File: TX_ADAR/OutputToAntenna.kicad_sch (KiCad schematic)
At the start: 8 parts, among them J10 Conn_Coaxial, J3 Conn_Coaxial, J4 Conn_Coaxial, J5 Conn_Coaxial, J6 Conn_Coaxial, J7 Conn_Coaxial, J8 Conn_Coaxial, J9 Conn_Coaxial

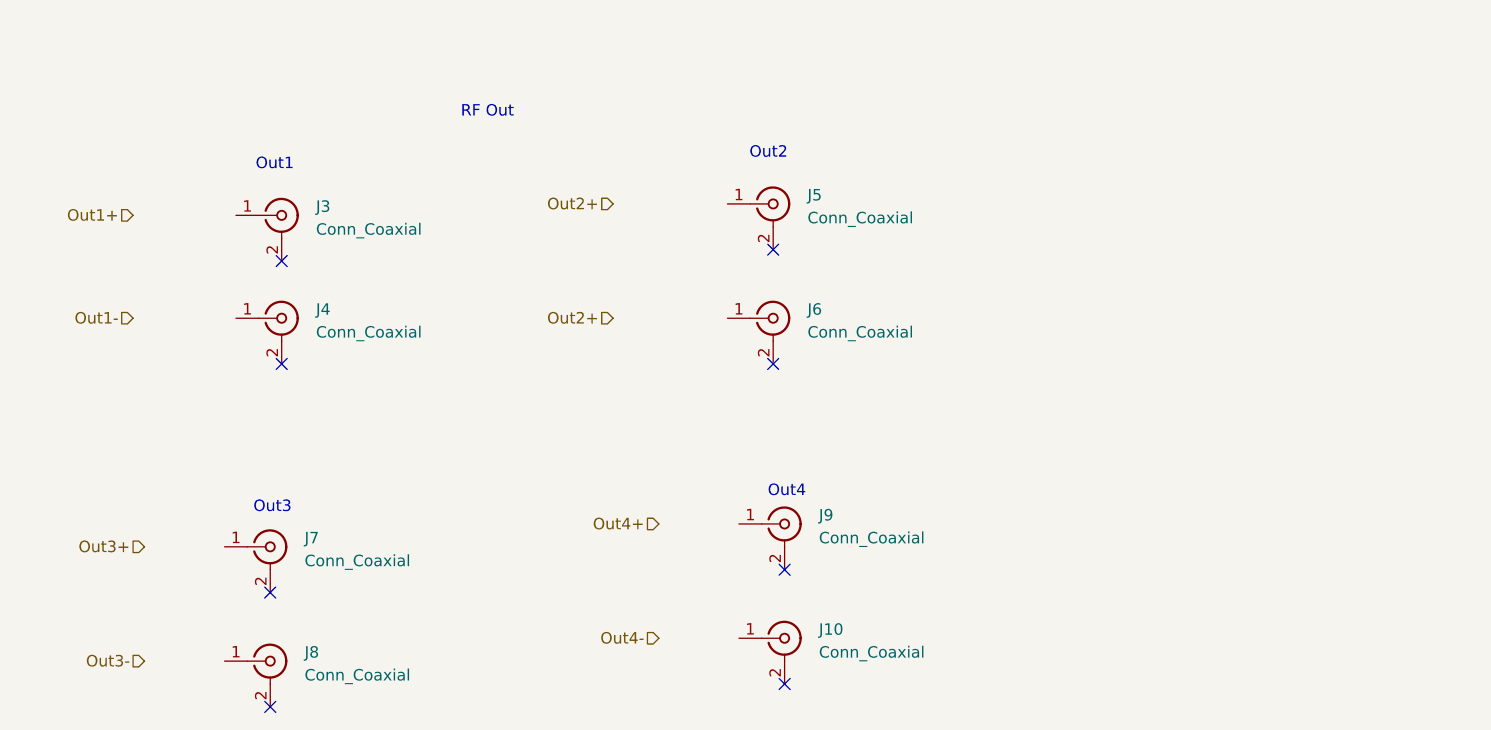
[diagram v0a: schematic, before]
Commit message: Cleaning up schematic
Added Cal Line
Connected RFOuts to connectors
Worked on State Machine connections
Finished connecting SDP Connector (need to double check)
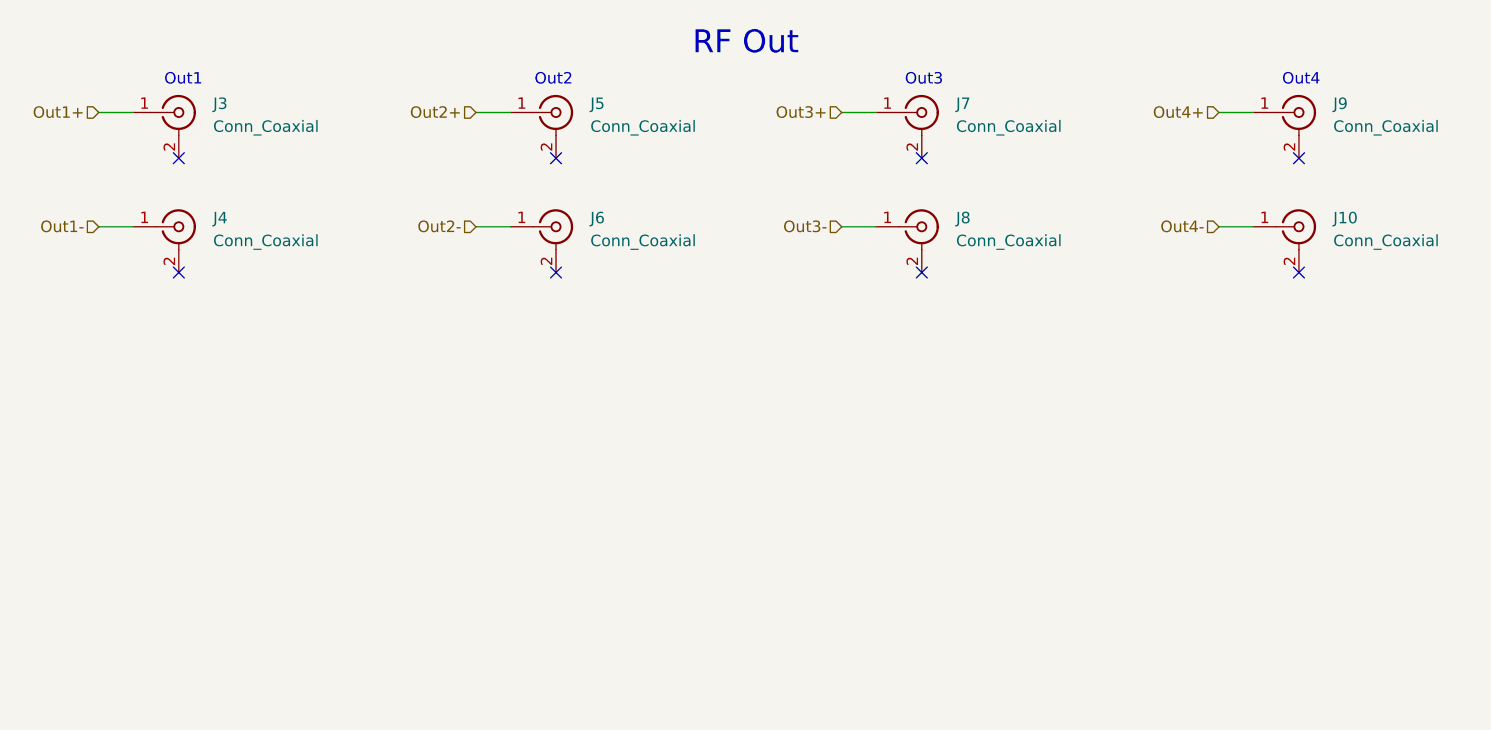
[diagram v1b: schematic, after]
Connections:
- net Out1+: now also J3.1 (In)
- net Out1-: now also J4.1 (In)
- net Out2+: now also J5.1 (In)
- net Out3+: now also J7.1 (In)
- net Out3-: now also J8.1 (In)
- net Out4+: now also J9.1 (In)
- net Out4-: now also J10.1 (In)
- net Out2-: now reaches J6.1 (In)
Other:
- moved on the sheet: J10, J3, J4, J5, J6, J7, J8, J9
